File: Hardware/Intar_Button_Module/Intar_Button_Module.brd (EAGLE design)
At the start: 17.8 x 25.9 mm, 11 parts, among them J1 GROVE-4P-2.0-3470130P1, SW1 SWITCH_MOMENTARY

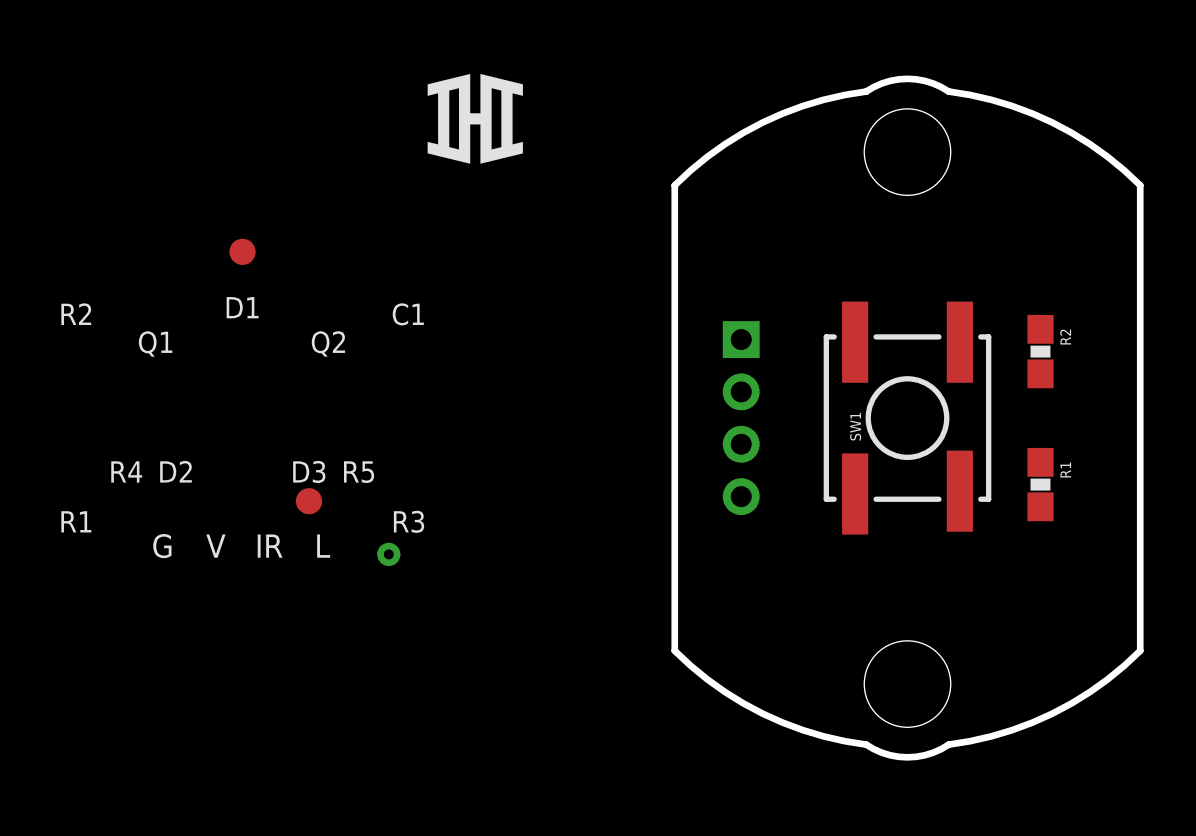
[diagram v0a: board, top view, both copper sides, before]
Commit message: Button module layout done.
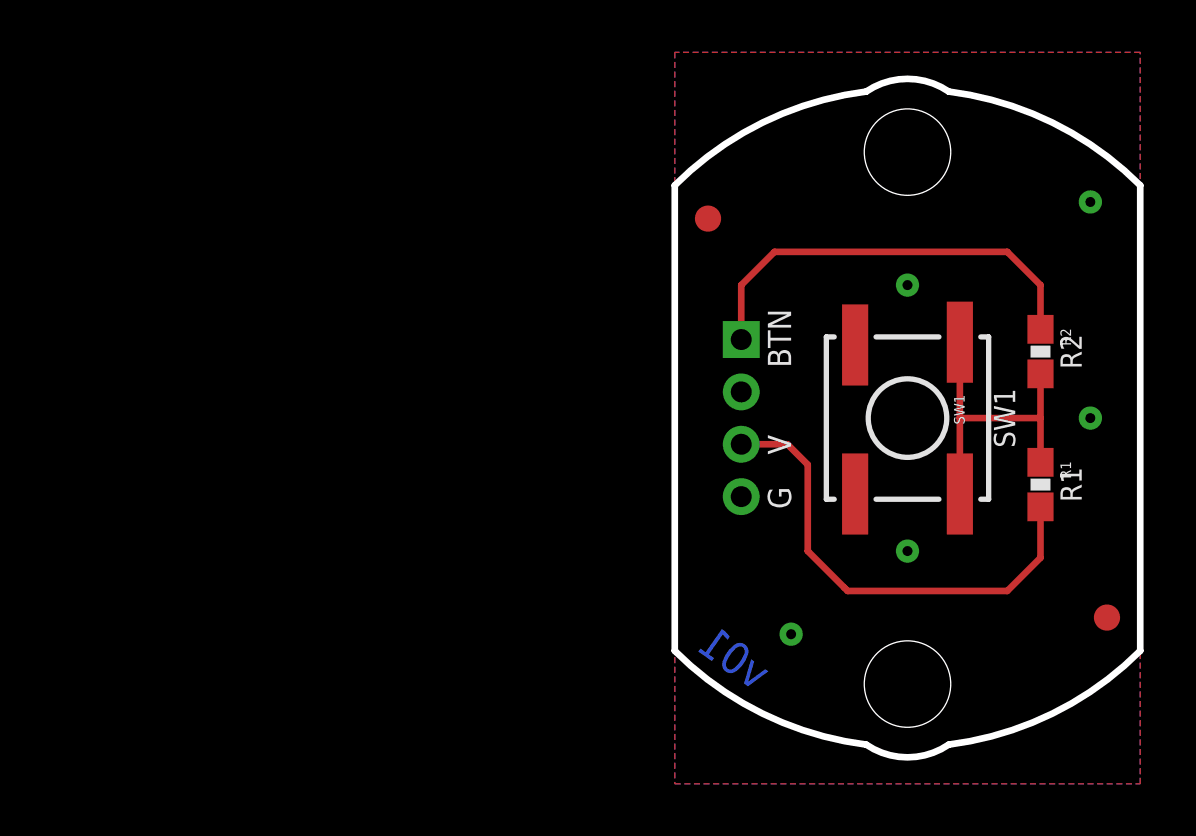
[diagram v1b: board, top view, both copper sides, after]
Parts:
- moved LOGO1 52.9 mm to (5.08, 8.26), turned to 270 degrees
- moved FID2 30.8 mm to (7.62, -7.62)
- moved U$1 29.2 mm to (5.08, -8.26), flipped to the bottom, turned to 270 degrees
- moved FID1 17.8 mm to (-7.62, 7.62)
- turned SW1 to 270 degrees
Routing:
- net VCC: track 0.00 -> 18.2 mm
- net BTN: track 0.00 -> 16.3 mm
- net N$1: track 0.00 -> 12.3 mm
- added copper zone on layer 1, net GND
- added copper zone on layer 16, net GND
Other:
- board text added: "BTN"
- board text added: "Intar Button Module"
- board text added: "SW1"
- board text removed: "C1"
- board text removed: "D1"
- board text removed: "D2"
- board text removed: "D3"
- board text removed: "IR"
- board text removed: "Intar IR LED Module"
- board text removed: "L"
- board text removed: "Q1"
- board text removed: "Q2"
- board text removed: "R3"
- board text removed: "R4"
- board text removed: "R5"
- board text removed: "Visible LEDs"

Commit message: Moved IHI and OSH logos away from name on all boards.
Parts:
- moved LOGO1 0.63 mm to (4.45, 8.26)
- moved U$1 0.63 mm to (4.45, -8.26)
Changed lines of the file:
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@@
 <setting verticaltext="up"/>
 </settings>
-<grid distance="0.05" unitdist="inch" unit="inch" style="dots" multiple="1" display="yes" altdistance="0.025" altunitdist="inch" altunit="inch"/>
+<grid distance="0.05" unitdist="inch" unit="inch" style="dots" multiple="1" display="yes" altdistance="0.005" altunitdist="inch" altunit="inch"/>
 <layers>
 <layer number="1" name="Top" color="4" fill="1" visible="yes" active="yes"/>
-<layer number="2" name="Route2" color="1" fill="3" visible="yes" active="yes"/>
-<layer number="15" name="Route15" color="4" fill="6" visible="yes" active="yes"/>
+<layer number="2" name="Route2" color="1" fill="3" visible="no" active="yes"/>
+<layer number="15" name="Route15" color="4" fill="6" visible="no" active="yes"/>
 <layer number="16" name="Bottom" color="1" fill="1" visible="yes" active="yes"/>
 <layer number="17" name="Pads" color="2" fill="1" visible="yes" active="yes"/>
@@
 <layer number="23" name="tOrigins" color="15" fill="1" visible="yes" active="yes"/>
 <layer number="24" name="bOrigins" color="15" fill="1" visible="yes" active="yes"/>
-<layer number="25" name="tNames" color="7" fill="1" visible="yes" active="yes"/>
-<layer number="26" name="bNames" color="7" fill="1" visible="yes" active="yes"/>
-<layer number="27" name="tValues" color="7" fill="1" visible="yes" active="yes"/>
-<layer number="28" name="bValues" color="7" fill="1" visible="yes" active="yes"/>
-<layer number="29" name="tStop" color="7" fill="3" visible="yes" active="yes"/>
-<layer number="30" name="bStop" color="7" fill="6" visible="yes" active="yes"/>
-<layer number="31" name="tCream" color="7" fill="4" visible="yes" active="yes"/>
-<layer number="32" name="bCream" color="7" fill="5" visible="yes" active="yes"/>
-<layer number="39" name="tKeepout" color="4" fill="11" visible="yes" active="yes"/>
-<layer number="40" name="bKeepout" color="1" fill="11" visible="yes" active="yes"/>
-<layer number="41" name="tRestrict" color="4" fill="10" visible="yes" active="yes"/>
-<layer number="42" name="bRestrict" color="1" fill="10" visible="yes" active="yes"/>
-<layer number="43" name="vRestrict" color="2" fill="10" visible="yes" active="yes"/>
-<layer number="44" name="Drills" color="7" fill="1" visible="yes" active="yes"/>
+<layer number="25" name="tNames" color="7" fill="1" visible="no" active="yes"/>
+<layer number="26" name="bNames" color="7" fill="1" visible="no" active="yes"/>
+<layer number="27" name="tValues" color="7" fill="1" visible="no" active="yes"/>
+<layer number="28" name="bValues" color="7" fill="1" visible="no" active="yes"/>
+<layer number="29" name="tStop" color="7" fill="3" visible="no" active="yes"/>
+<layer number="30" name="bStop" color="7" fill="6" visible="no" active="yes"/>
+<layer number="31" name="tCream" color="7" fill="4" visible="no" active="yes"/>
+<layer number="32" name="bCream" color="7" fill="5" visible="no" active="yes"/>
+<layer number="39" name="tKeepout" color="4" fill="11" visible="no" active="yes"/>
+<layer number="40" name="bKeepout" color="1" fill="11" visible="no" active="yes"/>
+<layer number="41" name="tRestrict" color="4" fill="10" visible="no" active="yes"/>
+<layer number="42" name="bRestrict" color="1" fill="10" visible="no" active="yes"/>
+<layer number="43" name="vRestrict" color="2" fill="10" visible="no" active="yes"/>
+<layer number="44" name="Drills" color="7" fill="1" visible="no" active="yes"/>
 <layer number="45" name="Holes" color="7" fill="1" visible="yes" active="yes"/>
-<layer number="46" name="Milling" color="3" fill="1" visible="yes" active="yes"/>
-<layer number="47" name="Measures" color="7" fill="1" visible="yes" active="yes"/>
+<layer number="46" name="Milling" color="3" fill="1" visible="no" active="yes"/>
+<layer number="47" name="Measures" color="7" fill="1" visible="no" active="yes"/>
 <layer number="51" name="tDocu" color="6" fill="1" visible="yes" active="yes"/>
-<layer number="52" name="bDocu" color="7" fill="1" visible="yes" active="yes"/>
+<layer number="52" name="bDocu" color="7" fill="1" visible="no" active="yes"/>
 <layer number="3" name="Route3" color="4" fill="3" visible="no" active="no"/>
 <layer number="4" name="Route4" color="1" fill="4" visible="no" active="no"/>
@@
 <element name="FRAME1" library="SparkFun-Aesthetics" package="CREATIVE_COMMONS" value="FRAME-LETTER" x="-33.02" y="-22.86"/>
 <element name="J1" library="Connector" package="4P-2.0" value="GROVE-4P-2.0-3470130P1" x="-6.35" y="0" rot="MR270"/>
-<element name="LOGO1" library="SparkFun-Aesthetics" package="OSHW-LOGO-S" value="OSHW-LOGOS" x="5.08" y="8.255" rot="SMR270"/>
+<element name="LOGO1" library="SparkFun-Aesthetics" package="OSHW-LOGO-S" value="OSHW-LOGOS" x="4.445" y="8.255" rot="SMR270"/>
 <element name="STANDOFF1" library="SparkFun-Electromechanical" package="STAND-OFF" value="STAND-OFF" x="0" y="-10.16"/>
 <element name="STANDOFF2" library="SparkFun-Electromechanical" package="STAND-OFF" value="STAND-OFF" x="0" y="10.16"/>
@@
 <attribute name="PROD_ID" value="RES-07863" x="5.08" y="2.54" size="1.778" layer="27" font="vector" ratio="15" rot="R270" display="off"/>
 </element>
-<element name="U$1" library="Intar_Eagle_Library" package="LOGO_SM" value="LOGOSM" x="5.08" y="-8.255" rot="MR270"/>
+<element name="U$1" library="Intar_Eagle_Library" package="LOGO_SM" value="LOGOSM" x="4.445" y="-8.255" rot="MR270"/>
 </elements>
 <signals>
